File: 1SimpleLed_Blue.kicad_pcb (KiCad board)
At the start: 2 copper layers, 30.2 x 30.2 mm, 17 parts, among them J1 JST_SH_SM06B-SRSS-TB_1x06-1MP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, J4 Conn_01x04, Q1 BSS84, U1 M24C02-FMN

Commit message: Change I2C pull-up resistors value to 4.7K
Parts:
- R5, R6: value 2.2K -> 4.7K
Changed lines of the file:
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@@
 			)
 		)
-		(property "Value" "2.2K"
+		(property "Value" "4.7K"
 			(at 0 1.43 90)
 			(layer "F.Fab")
@@
 			)
 		)
-		(property "Value" "2.2K"
+		(property "Value" "4.7K"
 			(at 0 1.43 90)
 			(layer "F.Fab")

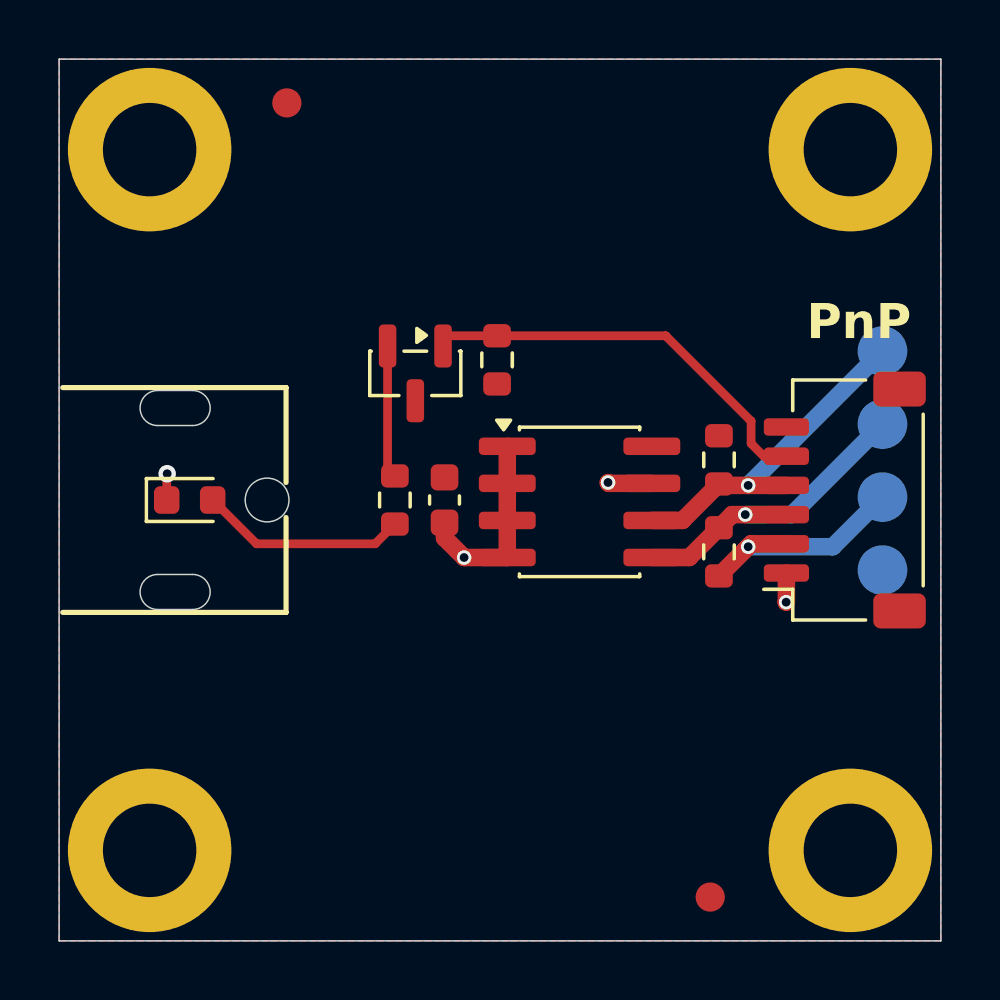
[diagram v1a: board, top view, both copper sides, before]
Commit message: Fix the design around MOSFET and add resistor in series to protect MCU's GPIO line
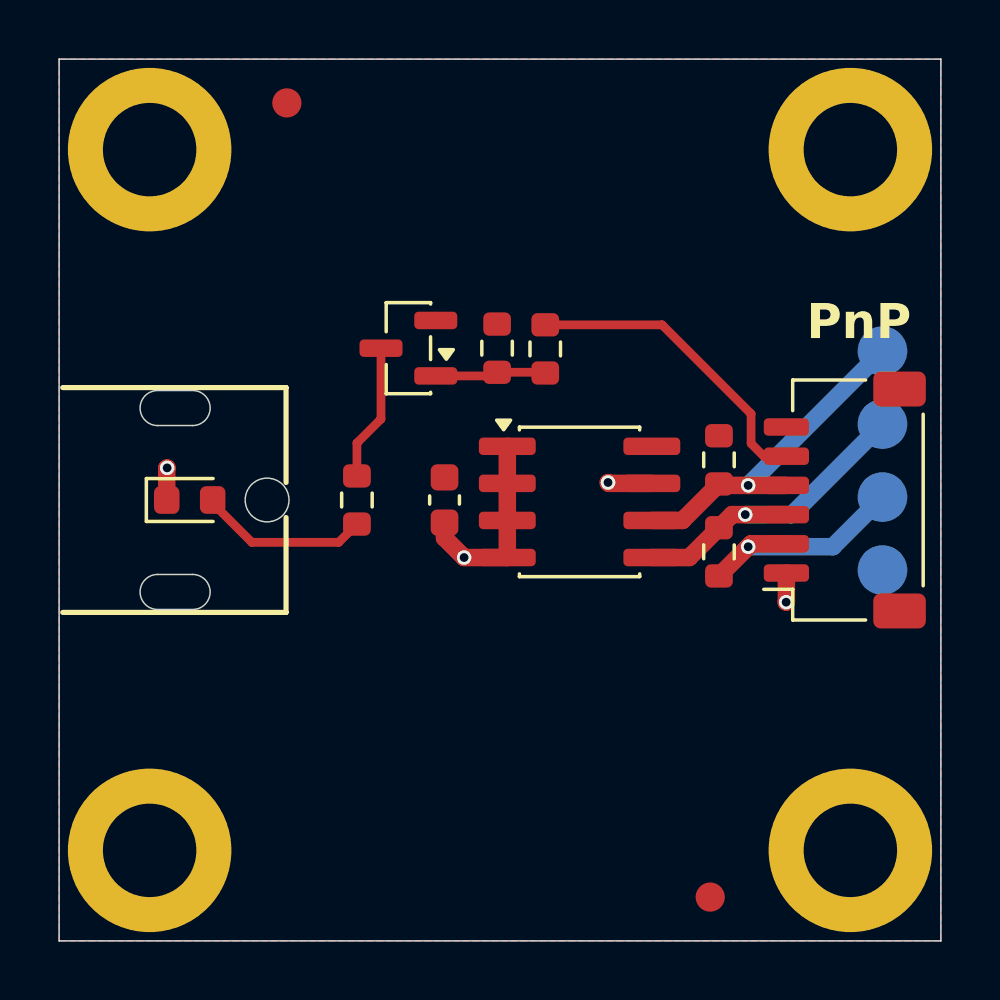
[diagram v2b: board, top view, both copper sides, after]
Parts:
- added R1: 330, Resistor_SMD:R_0603_1608Metric, F.Cu at (53.1, 41.9)
- moved R2 1.30 mm to (46.7, 47.1)
- moved Q1 0.89 mm to (48.5, 41.9), turned to 180 degrees
- moved R3 0.40 mm to (51.5, 41.9), turned to 90 degrees
- renumbered R23 to R2, R21 to R3
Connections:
- Q1 pad 1: INT1 -> Net-(Q1-G)
- Q1 pad 2: Net-(Q1-S) -> VCC
- Q1 pad 3: VCC -> Net-(Q1-D)
- R2 pad 1: Net-(Q1-S) -> Net-(Q1-D)
- R3 pad 1: INT1 -> Net-(Q1-G)
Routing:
- net Net-(Q1-D): track 0.00 -> 4.72 mm
- net Net-(Q1-S): track 4.55 -> 0.00 mm
- net Net-(Q1-G): track 0.00 -> 3.81 mm
- net INT1: track 13.9 -> 10.7 mm
- net Net-(D2-A): track 7.14 -> 5.75 mm
